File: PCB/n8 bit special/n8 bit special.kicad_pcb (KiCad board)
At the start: 4 copper layers, 99.9 x 100 mm, 50 parts, among them J1 USB_B_Micro, J2 PORT0, J3 PORT2, J4 PORT1, J6 Conn_02x08_Odd_Even, Q1 2N3904, SW1 SW_Push_Dual, U1 W65C02SxP, U10 74HC00, U2 CY62256-70PC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

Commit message: release candidate for v2
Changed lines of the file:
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@@
-(kicad_pcb (version 20171130) (host pcbnew "(5.1.9-0-10_14)")
+(kicad_pcb (version 20171130) (host pcbnew "(5.1.12-1-10_14)")
   (general
     (thickness 1.6)
@@
     )
   )
+  (gr_text GND (at 133.60908 130.90652) (layer F.SilkS)
+    (effects (font (size 0.8 0.8) (thickness 0.15)))
+  )
+  (gr_text ~RES (at 123.44908 130.90652) (layer F.SilkS)
+    (effects (font (size 0.8 0.8) (thickness 0.15)))
+  )
+  (gr_text +5V (at 130.89128 130.89382) (layer F.SilkS)
+    (effects (font (size 0.8 0.8) (thickness 0.15)))
+  )
+  (gr_text R~W (at 118.36908 130.90652) (layer F.SilkS)
+    (effects (font (size 0.8 0.8) (thickness 0.15)))
+  )
+  (gr_text A0 (at 100.58908 130.90652) (layer F.SilkS)
+    (effects (font (size 0.8 0.8) (thickness 0.15)))
+  )
+  (gr_text GND (at 98.04908 130.90652) (layer F.SilkS)
+    (effects (font (size 0.8 0.8) (thickness 0.15)))
+  )
+  (gr_text A2 (at 105.66908 130.90652) (layer F.SilkS)
+    (effects (font (size 0.8 0.8) (thickness 0.15)))
+  )
+  (gr_text +5V (at 95.33128 130.90652) (layer F.SilkS)
+    (effects (font (size 0.8 0.8) (thickness 0.15)))
+  )
+  (gr_text A1 (at 103.12908 130.90652) (layer F.SilkS)
+    (effects (font (size 0.8 0.8) (thickness 0.15)))
+  )
+  (gr_text F1 (at 128.52908 130.90652) (layer F.SilkS)
+    (effects (font (size 0.8 0.8) (thickness 0.15)))
+  )
+  (gr_text CLK (at 120.90908 130.90652) (layer F.SilkS)
+    (effects (font (size 0.8 0.8) (thickness 0.15)))
+  )
+  (gr_text F0 (at 125.98908 130.90652) (layer F.SilkS)
+    (effects (font (size 0.8 0.8) (thickness 0.15)))
+  )
+  (gr_text A3 (at 108.20908 130.90652) (layer F.SilkS)
+    (effects (font (size 0.8 0.8) (thickness 0.15)))
+  )
+  (gr_text ~CS (at 115.82908 130.90652) (layer F.SilkS)
+    (effects (font (size 0.8 0.8) (thickness 0.15)))
+  )
+  (gr_text A5 (at 113.28908 130.90652) (layer F.SilkS)
+    (effects (font (size 0.8 0.8) (thickness 0.15)))
+  )
+  (gr_text "A4\n" (at 110.74908 130.90652) (layer F.SilkS)
+    (effects (font (size 0.8 0.8) (thickness 0.15)))
+  )
   (gr_text JLCJLCJLCJLC (at 121.7041 45.1231) (layer F.SilkS)
     (effects (font (size 1 1) (thickness 0.15)))
@@
   (gr_arc (start 87.6935 139.192) (end 86.995 139.192) (angle -90) (layer Edge.Cuts) (width 0.1))
   (gr_arc (start 186.2455 139.192) (end 186.2455 139.8905) (angle -90) (layer Edge.Cuts) (width 0.1))
-  (gr_arc (start 87.6935 40.5765) (end 87.6935 39.878) (angle -90) (layer Edge.Cuts) (width 0.1))
-  (gr_arc (start 186.2455 40.5765) (end 186.944 40.5765) (angle -90) (layer Edge.Cuts) (width 0.1))
+  (gr_arc (start 87.6935 40.5892) (end 87.6935 39.8907) (angle -90) (layer Edge.Cuts) (width 0.1))
+  (gr_arc (start 186.2455 40.5892) (end 186.944 40.5892) (angle -90) (layer Edge.Cuts) (width 0.1))
   (gr_text 220 (at 173.8503 126.873 90) (layer F.SilkS)
     (effects (font (size 0.8 0.8) (thickness 0.15)))
@@
     (effects (font (size 0.8 0.8) (thickness 0.15)))
   )
-  (gr_text GND (at 133.60908 130.90652) (layer F.SilkS)
-    (effects (font (size 0.8 0.8) (thickness 0.15)))
-  )
-  (gr_text ~RES (at 123.44908 130.90652) (layer F.SilkS)
-    (effects (font (size 0.8 0.8) (thickness 0.15)))
-  )
-  (gr_text +5V (at 130.89128 130.89382) (layer F.SilkS)
-    (effects (font (size 0.8 0.8) (thickness 0.15)))
-  )
-  (gr_text R~W (at 118.36908 130.90652) (layer F.SilkS)
-    (effects (font (size 0.8 0.8) (thickness 0.15)))
-  )
-  (gr_text A0 (at 100.58908 130.90652) (layer F.SilkS)
-    (effects (font (size 0.8 0.8) (thickness 0.15)))
-  )
-  (gr_text GND (at 98.04908 130.90652) (layer F.SilkS)
-    (effects (font (size 0.8 0.8) (thickness 0.15)))
-  )
-  (gr_text A2 (at 105.66908 130.90652) (layer F.SilkS)
-    (effects (font (size 0.8 0.8) (thickness 0.15)))
-  )
-  (gr_text +5V (at 95.33128 130.90652) (layer F.SilkS)
-    (effects (font (size 0.8 0.8) (thickness 0.15)))
-  )
-  (gr_text A1 (at 103.12908 130.90652) (layer F.SilkS)
-    (effects (font (size 0.8 0.8) (thickness 0.15)))
-  )
-  (gr_text F1 (at 128.52908 130.90652) (layer F.SilkS)
-    (effects (font (size 0.8 0.8) (thickness 0.15)))
-  )
-  (gr_text CLK (at 120.90908 130.90652) (layer F.SilkS)
-    (effects (font (size 0.8 0.8) (thickness 0.15)))
-  )
-  (gr_text F0 (at 125.98908 130.90652) (layer F.SilkS)
-    (effects (font (size 0.8 0.8) (thickness 0.15)))
-  )
-  (gr_text A3 (at 108.20908 130.90652) (layer F.SilkS)
-    (effects (font (size 0.8 0.8) (thickness 0.15)))
-  )
-  (gr_text ~CS (at 115.82908 130.90652) (layer F.SilkS)
-    (effects (font (size 0.8 0.8) (thickness 0.15)))
-  )
-  (gr_text A5 (at 113.28908 130.90652) (layer F.SilkS)
-    (effects (font (size 0.8 0.8) (thickness 0.15)))
-  )
-  (gr_text "A4\n" (at 110.74908 130.90652) (layer F.SilkS)
-    (effects (font (size 0.8 0.8) (thickness 0.15)))
-  )
-  (gr_text GND (at 133.75386 113.1316) (layer F.SilkS)
+  (gr_text GND (at 133.6675 113.1189) (layer F.SilkS)
     (effects (font (size 0.8 0.8) (thickness 0.15)))
   )
-  (gr_text ~RES (at 123.53036 113.1316) (layer F.SilkS)
+  (gr_text ~RES (at 123.4821 113.1316) (layer F.SilkS)
     (effects (font (size 0.8 0.8) (thickness 0.15)))
   )
@@
     (effects (font (size 0.8 0.8) (thickness 0.15)))
   )
-  (gr_text R~W (at 118.45036 113.1316) (layer F.SilkS)
+  (gr_text R~W (at 118.4148 113.1316) (layer F.SilkS)
     (effects (font (size 0.8 0.8) (thickness 0.15)))
   )
@@
     (effects (font (size 0.8 0.8) (thickness 0.15)))
   )
-  (gr_text A2 (at 105.75036 113.1316) (layer F.SilkS)
+  (gr_text A2 (at 105.7021 113.1316) (layer F.SilkS)
     (effects (font (size 0.8 0.8) (thickness 0.15)))
   )
@@
     (effects (font (size 0.8 0.8) (thickness 0.15)))
   )
-  (gr_text A1 (at 103.21036 113.1316) (layer F.SilkS)
+  (gr_text A1 (at 103.1494 113.1316) (layer F.SilkS)
     (effects (font (size 0.8 0.8) (thickness 0.15)))
   )
-  (gr_text F1 (at 128.61036 113.1316) (layer F.SilkS)
+  (gr_text F1 (at 128.5621 113.1189) (layer F.SilkS)
     (effects (font (size 0.8 0.8) (thickness 0.15)))
   )
-  (gr_text CLK (at 120.99036 113.1316) (layer F.SilkS)
+  (gr_text CLK (at 120.9675 113.1316) (layer F.SilkS)
     (effects (font (size 0.8 0.8) (thickness 0.15)))
   )
-  (gr_text F0 (at 126.07036 113.0681) (layer F.SilkS)
+  (gr_text F0 (at 126.0094 113.0681) (layer F.SilkS)
     (effects (font (size 0.8 0.8) (thickness 0.15)))
   )
-  (gr_text A3 (at 108.29036 113.1316) (layer F.SilkS)
+  (gr_text A3 (at 108.2548 113.1316) (layer F.SilkS)
     (effects (font (size 0.8 0.8) (thickness 0.15)))
   )
-  (gr_text ~CS (at 115.91036 113.1316) (layer F.SilkS)
+  (gr_text ~CS (at 115.8621 113.1316) (layer F.SilkS)
     (effects (font (size 0.8 0.8) (thickness 0.15)))
   )
-  (gr_text A5 (at 113.37036 113.1316) (layer F.SilkS)
+  (gr_text A5 (at 113.3348 113.1316) (layer F.SilkS)
     (effects (font (size 0.8 0.8) (thickness 0.15)))
   )
-  (gr_text "A4\n" (at 110.83036 113.1316) (layer F.SilkS)
+  (gr_text "A4\n" (at 110.7821 113.1316) (layer F.SilkS)
     (effects (font (size 0.8 0.8) (thickness 0.15)))
   )
@@
     (effects (font (size 0.8 0.8) (thickness 0.15)))
   )
-  (gr_line (start 186.944 40.5765) (end 186.944 139.192) (layer Edge.Cuts) (width 0.1))
-  (gr_line (start 87.6935 39.878) (end 186.2455 39.878) (layer Edge.Cuts) (width 0.1))
-  (gr_line (start 86.995 139.192) (end 86.995 40.5765) (layer Edge.Cuts) (width 0.1))
+  (gr_line (start 186.944 40.5892) (end 186.944 139.192) (layer Edge.Cuts) (width 0.1))
+  (gr_line (start 87.6935 39.8907) (end 186.2455 39.8907) (layer Edge.Cuts) (width 0.1))
+  (gr_line (start 86.995 139.192) (end 86.995 40.5892) (layer Edge.Cuts) (width 0.1))
   (gr_line (start 186.2455 139.8905) (end 87.6935 139.8905) (layer Edge.Cuts) (width 0.1))
   (dimension 100.012501 (width 0.15) (layer Dwgs.User)

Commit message: v2 changes
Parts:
- U9: footprint Package_SO:SSOP-16_3.9x4.9mm_P0.635mm -> graphics:SSOP-16_3.9x4.9mm_P0.635mm_long_pads
- renumbered G*** to G1, G*** to G2
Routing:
- net +3V3: track 33.2 -> 36.3 mm
- net GND: track 4.26 -> 4.81 mm

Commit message: Converted USB chip to CH340C which is more available Converted USB chip to CH340C which is more available and easier to solder :)
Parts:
- removed C19, C20: 47pF, Capacitor_THT:C_Disc_D5.0mm_W2.5mm_P2.50mm
- removed R6: 220, Resistor_THT:R_Axial_DIN0207_L6.3mm_D2.5mm_P7.62mm_Horizontal
- removed R7, R8: 27, Resistor_THT:R_Axial_DIN0207_L6.3mm_D2.5mm_P7.62mm_Horizontal
- removed the U9 at (161.7, 112.5)
- added C10: 100nF, Capacitor_THT:C_Disc_D5.0mm_W2.5mm_P2.50mm, F.Cu at (177.2, 115.0)
- added R3: 220, Resistor_THT:R_Axial_DIN0207_L6.3mm_D2.5mm_P7.62mm_Horizontal, F.Cu at (175.9, 97.0)
- added U8: CH340C, Package_SO:SOIC-16_3.9x9.9mm_P1.27mm, F.Cu at (170.2, 113.7)
- D2: value TX -> LED_ALT
- D3: value RX -> LED_ALT
- J1: footprint Connector_USB:USB_Micro-B_Amphenol_10118194_Horizontal -> Connector_USB:USB_Micro-B_Wuerth_629105150521
- moved C18 11.7 mm to (163.2, 117.5)
- moved D3 6.20 mm to (179.7, 103.0)
- moved R5 6.11 mm to (175.9, 103.0), turned to 180 degrees
- moved D2 5.95 mm to (179.7, 97.0)
- moved J1 1.07 mm to (183.1, 112.2)
- renumbered J4 to J3, J3 to J4, U8 to U5, U5 to U9
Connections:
- net R~W renamed R~{W}
- net ~IRQ renamed ~{IRQ}
- net ~NMI renamed ~{NMI}
- net ~PORT0_CS renamed ~{PORT0_CS}
- net ~PORT1_CS renamed ~{PORT1_CS}
- net ~PORT2_CS renamed ~{PORT2_CS}
- net ~RAM1_CS renamed ~{RAM1_CS}
- net ~RAM2_CS renamed ~{RAM2_CS}
- net ~READ renamed ~{READ}
- net ~RES renamed ~{RES}
- net ~ROM_CS renamed ~{ROM_CS}
- net ~UART_CS renamed ~{UART_CS}
- net ~UART_IRQ renamed ~{UART_IRQ}
- net ~WRITE renamed ~{WRITE}
- C18 pad 1: +3V3 -> +5V
- D2 pad 2: Net-(D2-Pad2) -> +5V
- D3 pad 2: Net-(D3-Pad2) -> +5V
- J1 pad 4: Net-(J1-Pad4) -> unconnected-(J1-Pad4)
- J1 pad 6: Net-(J1-Pad6) -> unconnected-(J1-Pad6)
- J6 pad 2: Net-(J6-Pad2) -> Net-(RN1-Pad3)
- R5 pad 1: +3V3 -> Net-(D3-Pad1)
- R5 pad 2: Net-(D2-Pad2) -> TxD
- RN1 pad 3: BE_PULLUP -> Net-(RN1-Pad3)
- RN1 pad 4: Net-(J6-Pad2) -> Net-(J6-Pad4)
- RN1 pad 5: Net-(J6-Pad4) -> Net-(J6-Pad6)
- RN1 pad 6: Net-(J6-Pad6) -> Net-(J6-Pad8)
- RN1 pad 7: Net-(J6-Pad8) -> Net-(J6-Pad10)
- RN1 pad 8: Net-(J6-Pad10) -> Net-(J6-Pad12)
- RN1 pad 9: Net-(J6-Pad12) -> BE_PULLUP
- U1 pad 12: Net-(U1-Pad12) -> unconnected-(U1-Pad12)
- U1 pad 2: Net-(U1-Pad2) -> unconnected-(U1-Pad2)
- U1 pad 39: Net-(U1-Pad39) -> unconnected-(U1-Pad39)
- U1 pad 4: Net-(U1-Pad4) -> unconnected-(U1-Pad4)
- U1 pad 43: Net-(U1-Pad43) -> unconnected-(U1-Pad43)
- U1 pad 6: Net-(U1-Pad6) -> unconnected-(U1-Pad6)
- U1 pad 8: Net-(U1-Pad8) -> unconnected-(U1-Pad8)
- U5 pad 1: Net-(U8-Pad1) -> unconnected-(U5-Pad1)
- U5 pad 11: Net-(U8-Pad11) -> unconnected-(U5-Pad11)
- U5 pad 13: Net-(U8-Pad13) -> unconnected-(U5-Pad13)
- U5 pad 14: Net-(U8-Pad14) -> unconnected-(U5-Pad14)
- U5 pad 15: Net-(U8-Pad15) -> unconnected-(U5-Pad15)
- U5 pad 16: Net-(U8-Pad16) -> unconnected-(U5-Pad16)
- U5 pad 17: Net-(U8-Pad17) -> unconnected-(U5-Pad17)
- U5 pad 23: Net-(U8-Pad23) -> unconnected-(U5-Pad23)
- U5 pad 29: Net-(U8-Pad29) -> unconnected-(U5-Pad29)
- U5 pad 3: Net-(U8-Pad3) -> unconnected-(U5-Pad3)
- U5 pad 30: Net-(U8-Pad30) -> unconnected-(U5-Pad30)
- U5 pad 31: Net-(U8-Pad31) -> unconnected-(U5-Pad31)
- U5 pad 32: ~RTS -> ~{RTS}
- U5 pad 34: Net-(U8-Pad34) -> unconnected-(U5-Pad34)
- U5 pad 37: Net-(U8-Pad37) -> unconnected-(U5-Pad37)
- U5 pad 40: Net-(U8-Pad40) -> unconnected-(U5-Pad40)
- U5 pad 41: Net-(U8-Pad41) -> unconnected-(U5-Pad41)
- U5 pad 42: Net-(U8-Pad42) -> unconnected-(U5-Pad42)
- U5 pad 43: Net-(U8-Pad43) -> unconnected-(U5-Pad43)
- U5 pad 5: Net-(U8-Pad5) -> unconnected-(U5-Pad5)
- U5 pad 8: ~CTS -> ~{CTS}
- U6 pad 16: Net-(U6-Pad16) -> unconnected-(U6-Pad16)
- X1 pad 1: Net-(X1-Pad1) -> unconnected-(X1-Pad1)
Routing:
- net ~RTS: track 46.1 -> 0.00 mm
- net ~{RTS}: track 0.00 -> 39.2 mm, vias 0 -> 2
- net +3V3: track 36.3 -> 0.00 mm
- net ~{CTS}: track 0.00 -> 31.5 mm
- net Net-(D3-Pad1): track 33.1 -> 3.82 mm
- net ~CTS: track 23.7 -> 0.00 mm
- net Net-(D2-Pad1): track 25.8 -> 3.81 mm
- net BE_PULLUP: track 113.9 -> 97.8 mm
- net unconnected-(J1-Pad6): track 0.00 -> 15.5 mm
- net Net-(J1-Pad6): track 13.4 -> 0.00 mm
- net /F_USB_D-: track 10.9 -> 0.00 mm
- net /F_USB_D+: track 10.4 -> 0.00 mm
- net RxD: track 40.8 -> 49.7 mm
- net Net-(D2-Pad2): track 7.21 -> 0.00 mm
- net Net-(D3-Pad2): track 7.18 -> 0.00 mm
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- added copper zone on In2.Cu, net +5V
- added copper zone on In1.Cu, net GND
- removed copper zone on PWR_PLANE, net +5V
- removed copper zone on GND_PLANE, net GND
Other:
- net class Default removed
- net class Power removed
- board text added: "R~{W}"
- board text added: "~{CS}"
- board text added: "~{IRQ}"
- board text added: "~{NMI}"
- board text added: "~{RD}"
- board text added: "~{RES}"
- board text added: "~{WR}"
- board text removed: "R~W"
- board text removed: "~CS"
- board text removed: "~IRQ"
- board text removed: "~NMI"
- board text removed: "~RD"
- board text removed: "~RES"
- board text removed: "~WR"

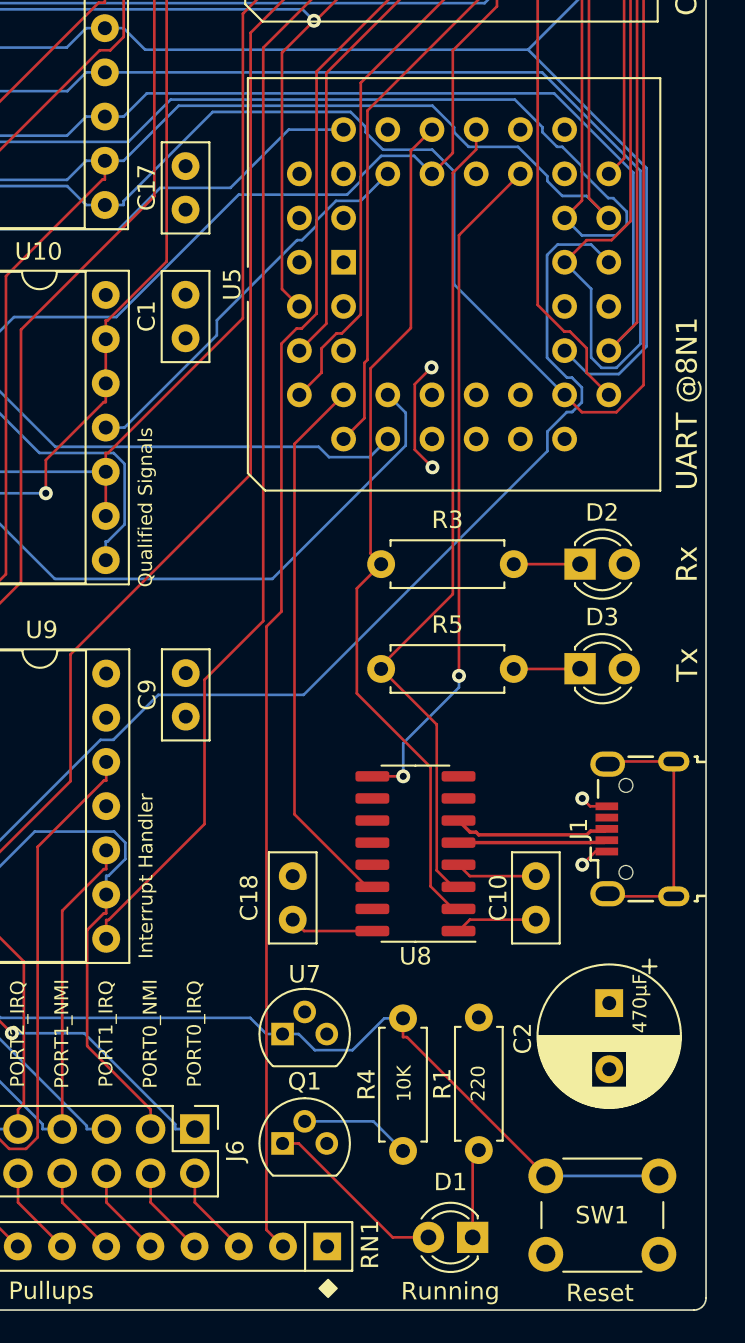
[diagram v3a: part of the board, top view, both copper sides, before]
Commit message: Fixed D+/D- miswiring
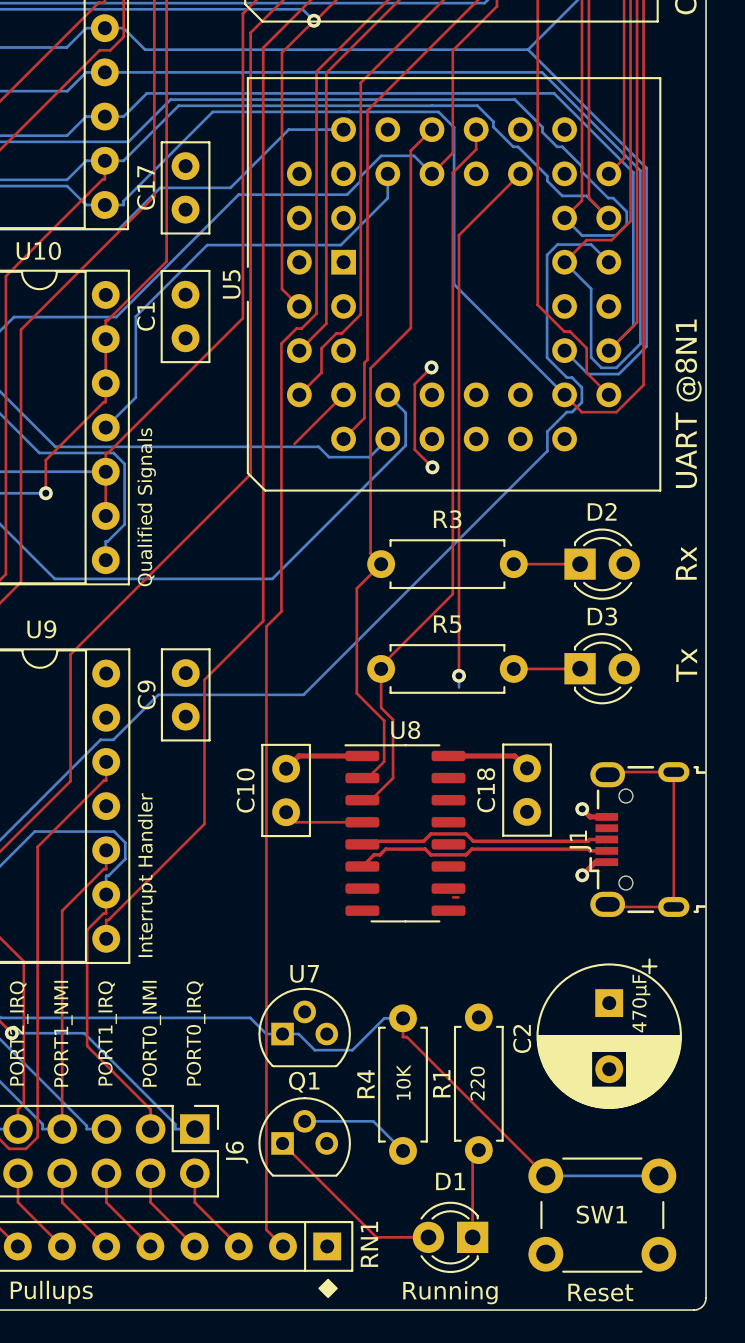
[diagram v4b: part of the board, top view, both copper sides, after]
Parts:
- moved C18 16.0 mm to (176.7, 108.8), turned to -90 degrees
- moved C10 14.8 mm to (162.8, 111.3), turned to 90 degrees
- moved U8 1.30 mm to (169.7, 112.5), turned to 0 degrees
- moved J1 0.61 mm to (183.1, 112.9)
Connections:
- U8 pad 5: USB_D- -> USB_D+
- U8 pad 6: USB_D+ -> USB_D-
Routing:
- net ~{CTS}: track 31.5 -> 3.99 mm
- net RxD: track 49.7 -> 40.9 mm
- net ~{RTS}: track 39.2 -> 31.3 mm, vias 2 -> 1
- net USB_D-: track 8.59 -> 14.8 mm
- net TxD: track 47.8 -> 42.1 mm
- net USB_D+: track 9.00 -> 14.5 mm
- net UART_RES: track 22.9 -> 25.8 mm
- net /D3: track 207.0 -> 208.5 mm
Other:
- board text added: "by Nate Rivard https://github.com/nrivard/n8-bit Version 3 May 2022"
- board text removed: "by Nate Rivard https://github.com/nrivard/n8-bit Version 2 Sept 2021"

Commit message: Final changes for v2
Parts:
- added REF**: MountingHole_3.2mm_M3, MountingHole:MountingHole_3.2mm_M3, F.Cu at (133.1, 39.3)
- added REF**: MountingHole_3.2mm_M3, MountingHole:MountingHole_3.2mm_M3, F.Cu at (91.3, 126.4)
- added REF**: MountingHole_3.2mm_M3, MountingHole:MountingHole_3.2mm_M3, F.Cu at (182.5, 126.3)
- moved C2 13.1 mm to (174.2, 111.3)
- moved C18 11.5 mm to (165.8, 105.0), turned to 180 degrees
- moved C10 5.83 mm to (157.0, 112.2)
- moved U8 5.20 mm to (164.5, 113.0)
- moved D2 1.30 mm to (181.0, 97.0)
- moved D3 1.30 mm to (181.0, 103.0)
- moved R3 1.30 mm to (177.2, 97.0)
- moved R5 1.30 mm to (177.2, 103.0)
- moved C13 0.93 mm to (133.2, 44.3)
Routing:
- net ~{CTS}: track 3.99 -> 33.0 mm
- net ~{RTS}: track 31.3 -> 48.1 mm, vias 1 -> 2
- net USB_D-: track 14.8 -> 21.4 mm
- net RxD: track 40.9 -> 46.2 mm
- net TxD: track 42.1 -> 47.3 mm
- net USB_D+: track 14.5 -> 19.5 mm
- net RDY_PULLUP: track 86.2 -> 91.1 mm
- net +5V: track 13.1 -> 12.3 mm
- net ~{WRITE}: track 157.7 -> 158.4 mm
- net GND: track 6.28 -> 5.71 mm
- net /A13: track 128.2 -> 128.8 mm

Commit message: rc1 before library swap test
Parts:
- moved REF** 0.58 mm to (133.1, 39.9)
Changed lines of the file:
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@@
   )
   (footprint "MountingHole:MountingHole_3.2mm_M3" (layer "F.Cu")
-    (at 133.1468 39.3192)
+    (at 133.1468 39.9)
     (descr "Mounting Hole 3.2mm, no annular, M3")
     (tags "mounting hole 3.2mm no annular m3")
